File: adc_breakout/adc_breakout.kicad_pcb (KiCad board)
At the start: 2 copper layers, 57.2 x 32 mm, 29 parts, among them IC101 PCM1863DBT, J101 Conn_Coaxial_x2, J102 Conn_01x02, J103 Conn_02x06_Odd_Even, U101 AZ1117-3.3, Y101 Crystal

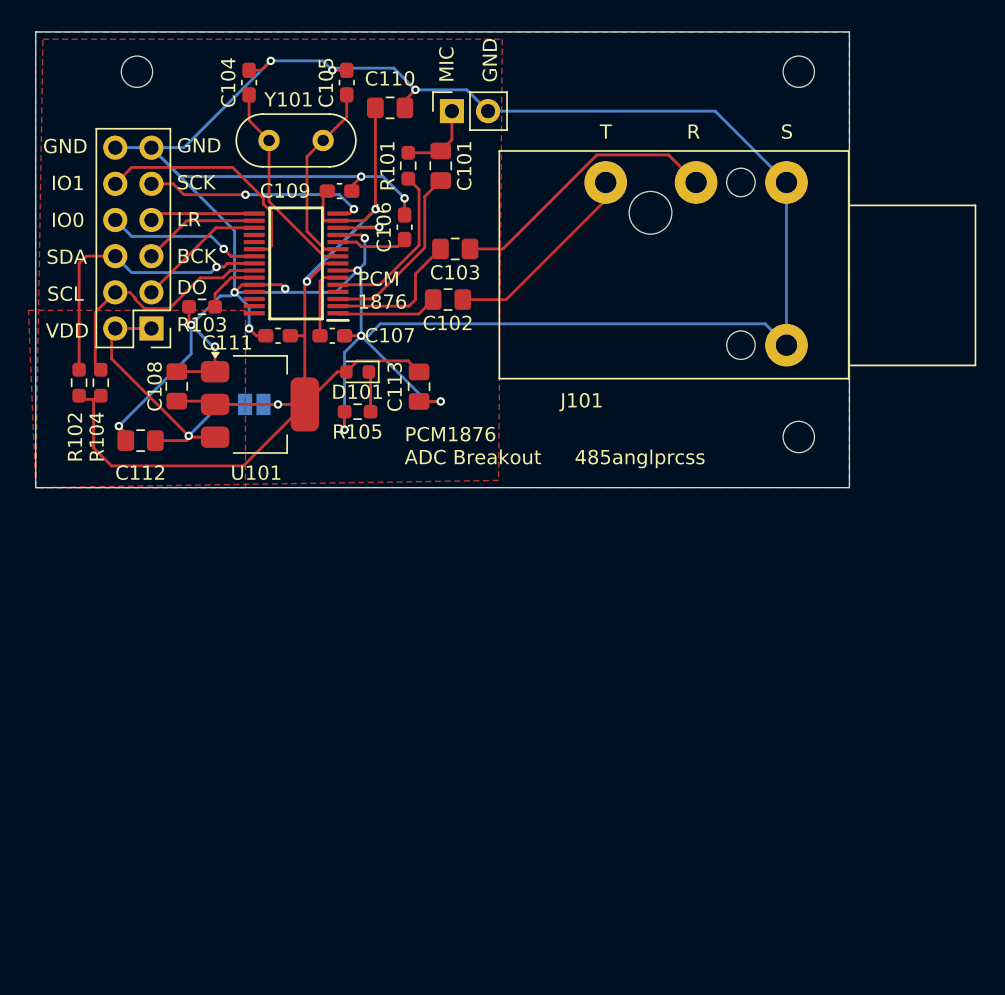
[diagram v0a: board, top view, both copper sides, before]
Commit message: Made breakboard compatible
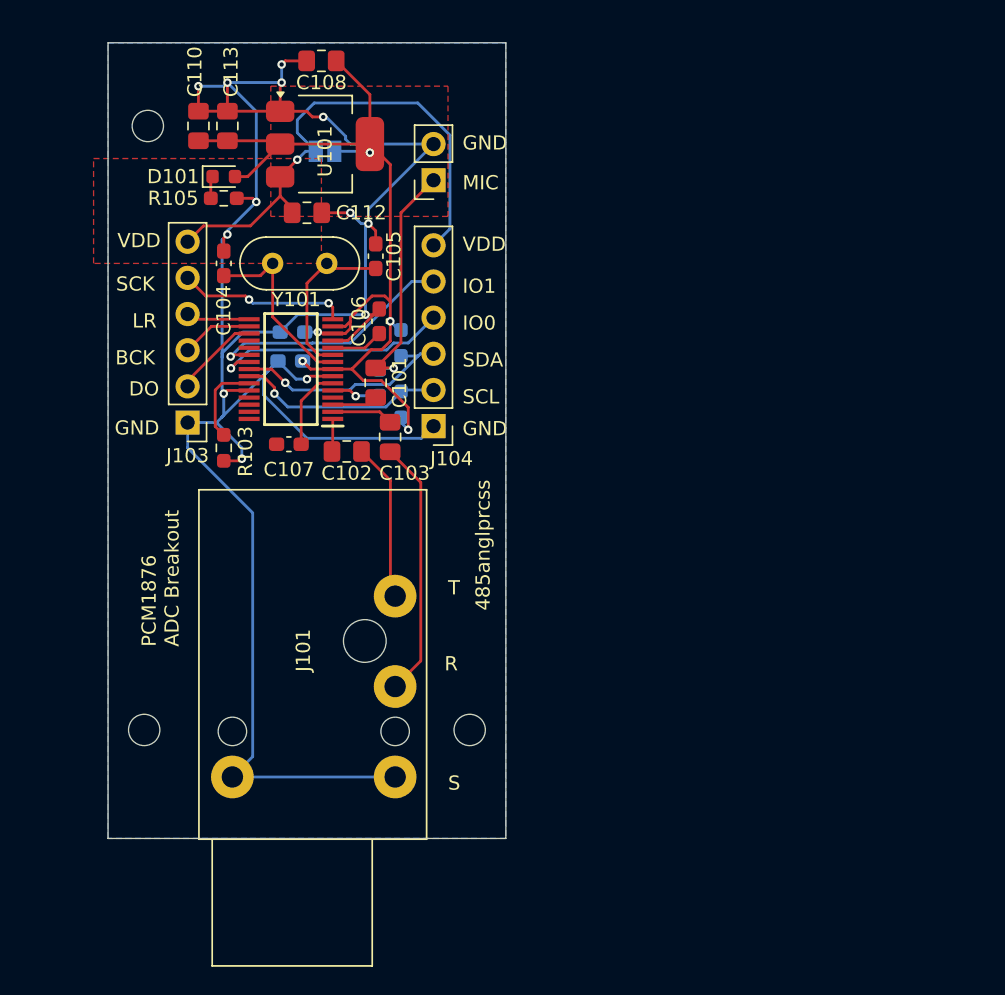
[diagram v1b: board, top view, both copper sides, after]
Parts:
- added J104: Conn_01x06, Connector_PinHeader_2.54mm:PinHeader_1x06_P2.54mm_Vertical, F.Cu at (165.1, 77.7)
- C109, C111, R101, R102, R104: moved to B.Cu
- J103: value Conn_02x06_Odd_Even -> Conn_01x06; footprint Connector_PinHeader_2.54mm:PinHeader_2x06_P2.54mm_Vertical -> Connector_PinHeader_2.54mm:PinHeader_1x06_P2.54mm_Vertical
- moved REF** 51.7 mm to (167.6, 99.1)
- moved REF** 50.4 mm to (144.8, 99.1)
- moved J101 32.6 mm to (162.4, 89.7), turned to -90 degrees
- moved C108 25.0 mm to (157.2, 52.1), turned to 0 degrees
- moved R102 22.8 mm to (162.8, 71.9), turned to 90 degrees
- moved C113 22.7 mm to (150.6, 56.6), turned to -90 degrees
- moved R104 21.1 mm to (162.8, 76.2)
- moved C112 19.8 mm to (156.2, 62.7), turned to 180 degrees
- moved U101 18.9 mm to (157.5, 57.9)
- moved JP101 18.5 mm to (157.5, 58.4)
- moved R105 17.7 mm to (150.4, 61.7), turned to 0 degrees
- moved D101 16.6 mm to (150.4, 60.2), turned to 0 degrees
- moved C101 15.9 mm to (161.0, 74.7)
- moved R101 15.4 mm to (161.3, 74.7)
- moved C103 14.0 mm to (162.1, 78.5), turned to 90 degrees
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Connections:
- J103 pad 1: VDD -> GND
- J103 pad 2: VDD -> /DOUT
- J103 pad 3: /DOUT -> /BCK
- J103 pad 4: /SCL -> /LRCK
- J103 pad 5: /BCK -> /SCK
- J103 pad 6: /SDA -> VDD
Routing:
- net GND: track 203.6 -> 170.9 mm, vias 16 -> 13
- net +3V3: track 84.1 -> 65.1 mm, vias 4 -> 5
- net VDD: track 21.7 -> 37.0 mm
- net /MIC_IN: track 5.46 -> 17.2 mm, vias 0 -> 1
- net /MIC: track 12.8 -> 3.22 mm
- net /MIC_BIAS: track 11.8 -> 3.45 mm, vias 0 -> 1
- net /GPIO0: track 10.8 -> 17.2 mm
- net /IN_R: track 9.92 -> 4.33 mm
- net /SDA: track 20.7 -> 15.8 mm
- net /IN_L: track 7.14 -> 2.31 mm
- net /SCK: track 16.2 -> 11.9 mm
- net /BCK: track 8.25 -> 5.01 mm
- net Net-(J101-IN1): track 14.2 -> 11.1 mm
- net /DOUT: track 9.10 -> 6.08 mm
- net /SCL: track 17.6 -> 14.6 mm, vias 0 -> 1
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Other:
- board size 57.2 x 32 mm -> 27.9 x 55.9 mm
- board text removed: "PCM 1876"
